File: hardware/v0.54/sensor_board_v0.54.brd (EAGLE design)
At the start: 56.4 x 41.7 mm, 59 parts, among them J3 USB-MICROB, J6 AVR_SPI_PRG_6PTH, U1 ATMEGA328P, U10 TSL2591, U3 OPA344, U4 RFM69HW, U5 FT231XS, U6 ADMP401, U8 MCP1703CB, U9 BMP280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

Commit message: BOM update
- Added MPN for 0.1 and 10uF
- Added I2C address and value for SHT35 on schematic
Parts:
- U2: value (none) -> SHT35
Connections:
- removed net A7: U1.22
- removed net D5: U1.9
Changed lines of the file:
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@@
 </element>
 <element name="C6" library="SparkFun-Capacitors" package="0805" value="0.1uF" x="4.2926" y="22.1234" smashed="yes" rot="R180">
-<attribute name="MPN" value="CC0805ZRY5V8BB105" x="4.2926" y="22.1234" size="1.778" layer="27" rot="R180" display="off"/>
+<attribute name="MPN" value="CC0805KRX7R9BB104" x="4.2926" y="22.1234" size="1.778" layer="27" rot="R180" display="off"/>
 <attribute name="NAME" x="2.4003" y="21.6154" size="0.6096" layer="121" font="vector" rot="R90"/>
 </element>
@@
 <attribute name="VALUE" x="51.308" y="21.7678" size="1.27" layer="27"/>
 </element>
-<element name="U2" library="Adafruit SHT31" package="SHT3X" value="" x="54.2544" y="43.7896" smashed="yes">
+<element name="U2" library="Adafruit SHT31" package="SHT3X" value="SHT35" x="54.2544" y="43.7896" smashed="yes">
 <attribute name="MPN" value="SHT35-DIS-B" x="54.2544" y="43.7896" size="1.778" layer="27" display="off"/>
 <attribute name="NAME" x="55.2754" y="45.5012" size="0.6096" layer="121" font="vector" align="bottom-center"/>
@@
 </element>
 <element name="C4" library="SparkFun-Capacitors" package="0805" value="10uF" x="4.2926" y="24.2316" smashed="yes" rot="R180">
-<attribute name="MPN" value="CC0805ZRY5V8BB105" x="4.2926" y="24.2316" size="1.778" layer="27" rot="R180" display="off"/>
+<attribute name="MPN" value="CC0805KKX5R6BB106" x="4.2926" y="24.2316" size="1.778" layer="27" rot="R180" display="off"/>
 <attribute name="NAME" x="1.7907" y="24.2062" size="0.6096" layer="121" font="vector" rot="R270" align="bottom-center"/>
 </element>
@@
 <wire x1="53.5432" y1="27.2796" x2="44.2468" y2="27.2796" width="0.1778" layer="16"/>
 </signal>
-<signal name="D5">
-<contactref element="U1" pad="9"/>
-</signal>
 <signal name="N$4">
 <contactref element="U1" pad="8"/>
@@
 <wire x1="12.0904" y1="34.2392" x2="6.35" y2="34.2392" width="0.1778" layer="16"/>
 </signal>
-<signal name="A7">
-<contactref element="U1" pad="22"/>
-</signal>
 <signal name="A0">

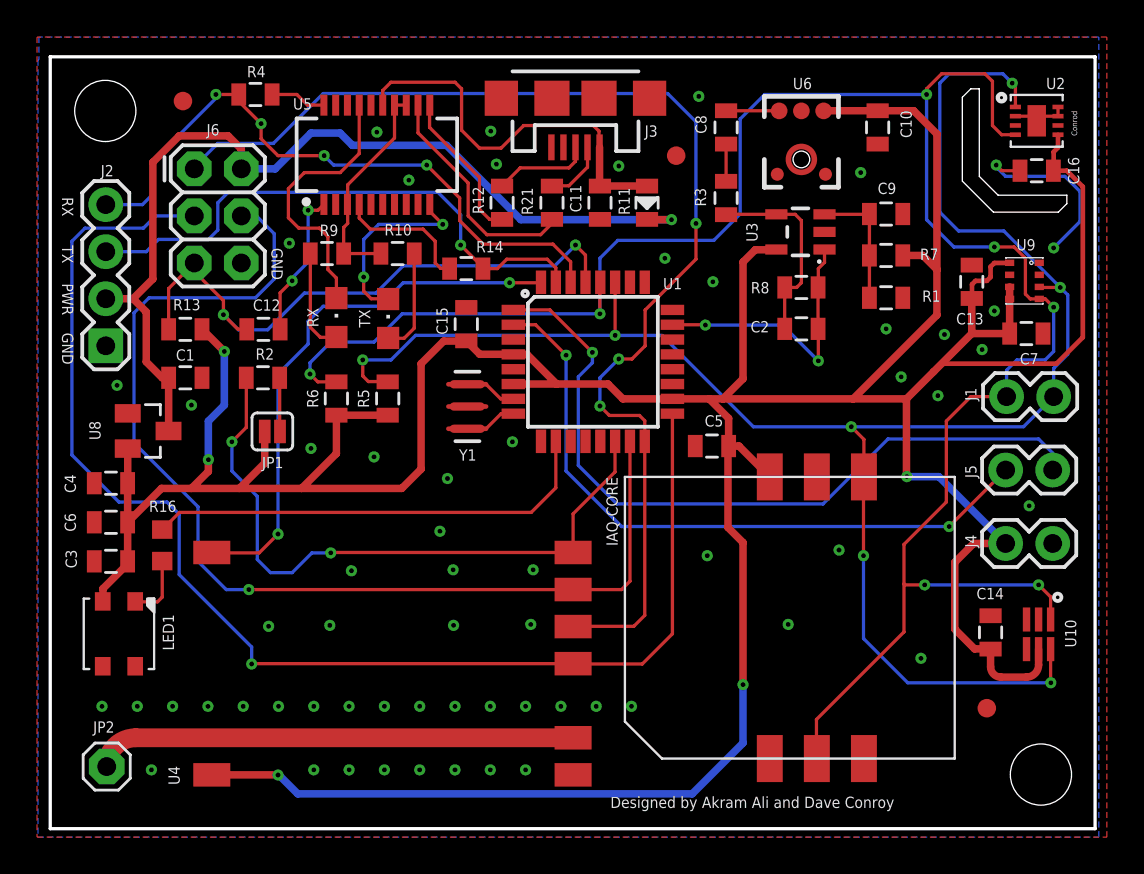
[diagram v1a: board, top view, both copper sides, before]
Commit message: trace adjustments
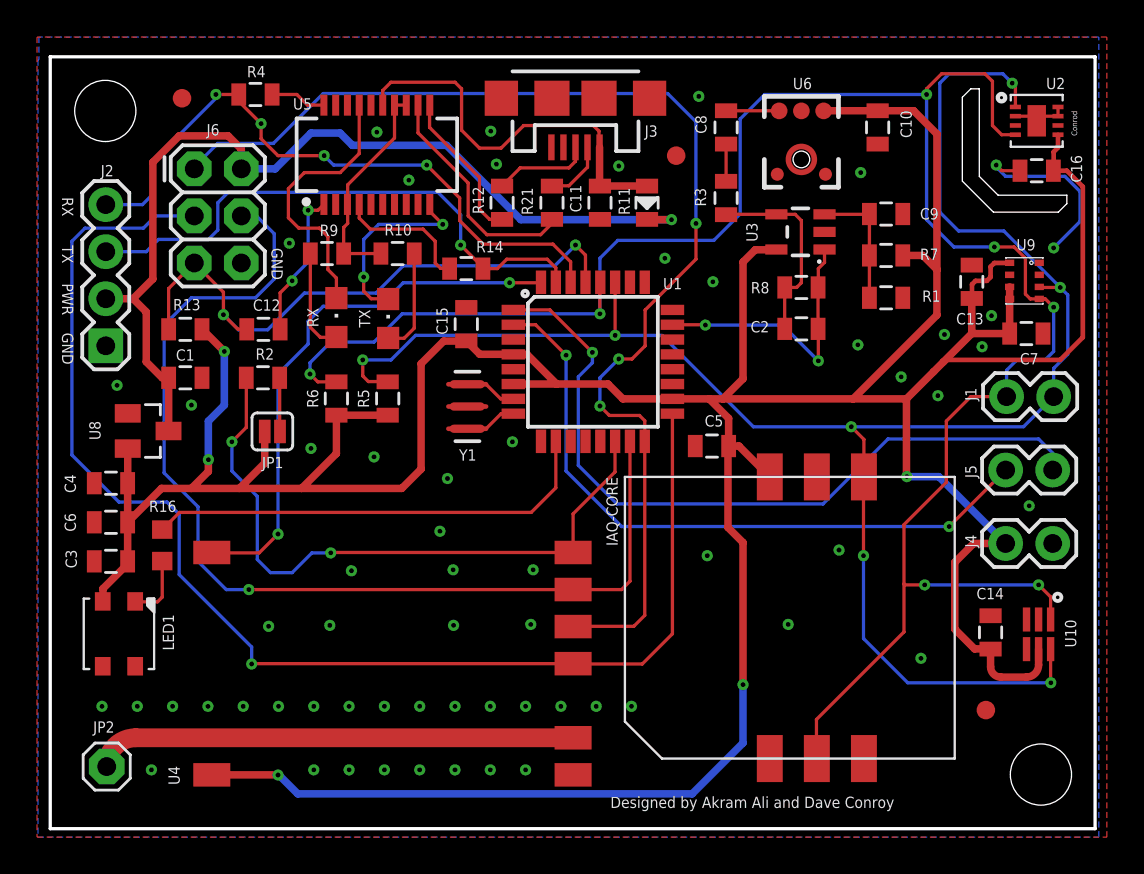
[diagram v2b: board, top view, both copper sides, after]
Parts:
- moved U$1 0.16 mm to (8.13, 45.0)
- moved U$2 0.11 mm to (51.5, 12.0)
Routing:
- net MOSI: track 59.5 -> 56.8 mm
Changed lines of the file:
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@@
 <?xml version="1.0" encoding="utf-8"?>
 <!DOCTYPE eagle SYSTEM "eagle.dtd">
-<eagle version="8.1.0">
+<eagle version="7.7.0">
 <drawing>
 <settings>
@@
 <element name="C9" library="SparkFun-Capacitors" package="0805" value="1uF" x="46.1264" y="38.7604" smashed="yes">
 <attribute name="MPN" value="CC0805ZRY5V8BB105" x="46.1264" y="38.7604" size="1.778" layer="27" display="off"/>
-<attribute name="NAME" x="45.6692" y="39.8399" size="0.6096" layer="121" font="vector"/>
+<attribute name="NAME" x="47.9552" y="38.4683" size="0.6096" layer="121" font="vector"/>
 </element>
 <element name="C10" library="SparkFun-Capacitors" package="0805" value="0.1uF" x="45.6692" y="43.434" smashed="yes" rot="R270">
@@
 <attribute name="VALUE" x="2.794" y="5.7658" size="1.27" layer="27"/>
 </element>
-<element name="U$1" library="adafruit" package="FIDUCIAL_1MM" value="FIDUCIAL" x="8.1788" y="44.8564"/>
-<element name="U$2" library="adafruit" package="FIDUCIAL_1MM" value="FIDUCIAL" x="51.562" y="12.0904"/>
+<element name="U$1" library="adafruit" package="FIDUCIAL_1MM" value="FIDUCIAL" x="8.128" y="45.0088"/>
+<element name="U$2" library="adafruit" package="FIDUCIAL_1MM" value="FIDUCIAL" x="51.5112" y="11.9888"/>
 <element name="U$3" library="adafruit" package="FIDUCIAL_1MM" value="FIDUCIAL" x="34.798" y="41.91"/>
 <element name="U10" library="TSL2591" package="DFN6_TAOS" value="TSL2591" x="54.356" y="16.0782" smashed="yes" rot="R270">
@@
 <element name="C16" library="SparkFun-Passives" package="0805" value="0.1uF" x="54.2544" y="41.0972" smashed="yes" rot="R180">
 <attribute name="MPN" value="CC0805KRX7R9BB104" x="54.2544" y="41.0972" size="1.778" layer="27" rot="R180" display="off"/>
-<attribute name="NAME" x="55.9435" y="41.0972" size="0.6096" layer="121" font="vector" rot="R270" align="bottom-center"/>
+<attribute name="NAME" x="56.0959" y="41.1988" size="0.6096" layer="121" font="vector" rot="R270" align="bottom-center"/>
 </element>
 <element name="J6" library="SparkFun-Connectors" package="2X3" value="AVR_SPI_PRG_6PTH" x="8.7884" y="41.1988" smashed="yes" rot="R270">
@@
 <via x="18.6436" y="43.18" extent="1-16" drill="0.254" diameter="0.127"/>
 <via x="49.276" y="32.258" extent="1-16" drill="0.254" diameter="0.127"/>
-<via x="46.1264" y="32.5628" extent="1-16" drill="0.254" diameter="0.127"/>
+<via x="44.6024" y="31.6992" extent="1-16" drill="0.254" diameter="0.127"/>
 <via x="48.9204" y="28.956" extent="1-16" drill="0.254" diameter="0.127"/>
 <via x="46.9392" y="29.972" extent="1-16" drill="0.254" diameter="0.127"/>
-<via x="51.308" y="31.4452" extent="1-16" drill="0.254" diameter="0.127"/>
+<via x="51.308" y="31.5976" extent="1-16" drill="0.254" diameter="0.127"/>
 <via x="24.7904" y="43.2308" extent="1-16" drill="0.254" diameter="0.127"/>
 <via x="25.0952" y="41.4528" extent="1-16" drill="0.254" diameter="0.127"/>
@@
 <via x="3.81" y="12.192" extent="1-16" drill="0.254" diameter="0.127"/>
 <via x="6.477" y="8.763" extent="1-16" drill="0.254" diameter="0.127"/>
-<via x="51.9684" y="33.528" extent="1-16" drill="0.254" diameter="0.127"/>
+<via x="51.816" y="33.274" extent="1-16" drill="0.254" diameter="0.127"/>
 <contactref element="U10" pad="3"/>
 <contactref element="C14" pad="1"/>
@@
 <wire x1="50.7636" y1="34.1884" x2="50.7492" y2="34.2028" width="0.4064" layer="1"/>
 <wire x1="47.2252" y1="28.7848" x2="48.6918" y2="30.2514" width="0.4064" layer="1"/>
-<wire x1="48.6918" y1="30.2514" x2="50.7492" y2="32.3088" width="0.4064" layer="1"/>
+<wire x1="48.6918" y1="30.2514" x2="49.2252" y2="30.7848" width="0.4064" layer="1"/>
+<wire x1="49.2252" y1="30.7848" x2="50.7492" y2="32.3088" width="0.4064" layer="1"/>
 <wire x1="45.6692" y1="44.334" x2="47.614" y2="44.334" width="0.4064" layer="1"/>
 <wire x1="47.614" y1="44.334" x2="48.8696" y2="43.0784" width="0.4064" layer="1"/>
@@
 <wire x1="55.1688" y1="42.1132" x2="55.1688" y2="41.1116" width="0.254" layer="1"/>
 <wire x1="55.1688" y1="41.1116" x2="55.1544" y2="41.0972" width="0.254" layer="1"/>
-<wire x1="55.3212" y1="30.6832" x2="49.1236" y2="30.6832" width="0.254" layer="1"/>
 <wire x1="49.1236" y1="30.6832" x2="48.6918" y2="30.2514" width="0.254" layer="1"/>
 <wire x1="47.2252" y1="28.7848" x2="47.2252" y2="24.606" width="0.4064" layer="1"/>
@@
 <wire x1="55.88" y1="41.0972" x2="56.7436" y2="40.2336" width="0.254" layer="1"/>
 <wire x1="56.7436" y1="40.2336" x2="56.7436" y2="32.1056" width="0.254" layer="1"/>
-<wire x1="56.7436" y1="32.1056" x2="55.3212" y2="30.6832" width="0.254" layer="1"/>
 <contactref element="C4" pad="1"/>
 <contactref element="C3" pad="1"/>
@@
 <wire x1="9.5504" y1="24.8666" x2="8.636" y2="23.9522" width="0.4064" layer="1"/>
 <wire x1="9.5504" y1="25.5016" x2="9.5504" y2="24.8666" width="0.4064" layer="1"/>
+<wire x1="56.7436" y1="32.1056" x2="55.5244" y2="30.8864" width="0.254" layer="1"/>
+<wire x1="55.5244" y1="30.8864" x2="49.3268" y2="30.8864" width="0.254" layer="1"/>
+<wire x1="49.3268" y1="30.8864" x2="49.2252" y2="30.7848" width="0.254" layer="1"/>
 </signal>
 <signal name="SCL">
@@
 <wire x1="52.6288" y1="28.9052" x2="50.6984" y2="28.9052" width="0.1778" layer="1"/>
 <wire x1="50.6984" y1="28.9052" x2="49.3776" y2="27.5844" width="0.1778" layer="1"/>
-<wire x1="49.3776" y1="27.5844" x2="49.3776" y2="23.2156" width="0.1778" layer="1"/>
-<wire x1="49.3776" y1="23.2156" x2="47.0916" y2="20.9296" width="0.1778" layer="1"/>
-<wire x1="47.0916" y1="20.9296" x2="47.0916" y2="18.796" width="0.1778" layer="1"/>
+<wire x1="47.0916" y1="21.9964" x2="47.0916" y2="18.796" width="0.1778" layer="1"/>
 <wire x1="47.0916" y1="18.796" x2="47.0916" y2="16.2052" width="0.1778" layer="1"/>
 <wire x1="47.0916" y1="16.2052" x2="42.3672" y2="11.4808" width="0.1778" layer="1"/>
@@
 <wire x1="51.8668" y1="45.9232" x2="51.4604" y2="46.3296" width="0.1778" layer="1"/>
 <wire x1="51.4604" y1="46.3296" x2="49.1236" y2="46.3296" width="0.1778" layer="1"/>
+<wire x1="47.0916" y1="21.9964" x2="49.3776" y2="24.2824" width="0.1778" layer="1"/>
+<wire x1="49.3776" y1="24.2824" x2="49.3776" y2="27.5844" width="0.1778" layer="1"/>
 </signal>
 <signal name="SDA">
@@
 <wire x1="29.9022" y1="36.5442" x2="29.9022" y2="35.0774" width="0.1778" layer="1"/>
 <contactref element="J6" pad="5"/>
-<wire x1="8.7376" y1="36.068" x2="8.7884" y2="36.1188" width="0.1778" layer="16"/>
 <wire x1="18.5928" y1="34.4932" x2="14.732" y2="34.4932" width="0.1778" layer="16"/>
-<wire x1="8.7884" y1="36.1188" x2="8.7884" y2="35.6616" width="0.1778" layer="1"/>
-<wire x1="8.7884" y1="35.6616" x2="10.3632" y2="34.0868" width="0.1778" layer="1"/>
 <wire x1="7.4058" y1="32.5374" x2="7.4058" y2="34.7362" width="0.1778" layer="1"/>
-<wire x1="7.4058" y1="34.7362" x2="8.7884" y2="36.1188" width="0.1778" layer="1"/>
 <wire x1="14.732" y1="34.4932" x2="12.7508" y2="32.512" width="0.1778" layer="16"/>
 <wire x1="12.7508" y1="32.512" x2="11.176" y2="32.512" width="0.1778" layer="16"/>
 <wire x1="11.176" y1="32.512" x2="10.3632" y2="33.3248" width="0.1778" layer="16"/>
 <via x="10.3632" y="33.3248" extent="1-16" drill="0.254" diameter="0.127"/>
-<wire x1="10.3632" y1="33.3248" x2="10.3632" y2="34.0868" width="0.1778" layer="1"/>
+<wire x1="10.3632" y1="33.3248" x2="10.3632" y2="34.544" width="0.1778" layer="1"/>
 <wire x1="11.6222" y1="32.5374" x2="11.1506" y2="32.5374" width="0.1778" layer="1"/>
 <wire x1="11.1506" y1="32.5374" x2="10.3632" y2="33.3248" width="0.1778" layer="1"/>
@@
 <wire x1="20.066" y1="35.9664" x2="28.2448" y2="35.9664" width="0.1778" layer="16"/>
 <wire x1="28.2448" y1="35.9664" x2="29.3624" y2="37.084" width="0.1778" layer="16"/>
+<wire x1="8.7884" y1="36.1188" x2="10.3632" y2="34.544" width="0.1778" layer="1"/>
+<wire x1="8.7884" y1="36.1188" x2="7.4058" y2="34.7362" width="0.1778" layer="1"/>
 </signal>
 <signal name="MOSI">
@@
 <via x="11.7348" y="18.4912" extent="1-16" drill="0.254" diameter="0.127"/>
 <wire x1="10.5156" y1="18.4912" x2="11.7348" y2="18.4912" width="0.1778" layer="16"/>
-<wire x1="5.5372" y1="33.4264" x2="5.5372" y2="26.416" width="0.1778" layer="16"/>
 <wire x1="31.8516" y1="18.4912" x2="29.2372" y2="18.4912" width="0.1778" layer="1"/>
 <wire x1="29.2372" y1="18.4912" x2="29.2344" y2="18.494" width="0.1778" layer="1"/>
@@
 <contactref element="J6" pad="4"/>
 <wire x1="11.3284" y1="38.7096" x2="11.3284" y2="38.6588" width="0.1778" layer="16"/>
-<wire x1="6.35" y1="34.2392" x2="5.5372" y2="33.4264" width="0.1778" layer="16"/>
-<wire x1="5.5372" y1="26.416" x2="8.9916" y2="22.9616" width="0.1778" layer="16"/>
 <wire x1="8.9916" y1="22.9616" x2="8.9916" y2="20.0152" width="0.1778" layer="16"/>
 <wire x1="11.3284" y1="38.6588" x2="12.1412" y2="38.6588" width="0.1778" layer="16"/>
@@
 <wire x1="13.1064" y1="37.6936" x2="13.1064" y2="35.2552" width="0.1778" layer="16"/>
 <wire x1="13.1064" y1="35.2552" x2="12.0904" y2="34.2392" width="0.1778" layer="16"/>
-<wire x1="12.0904" y1="34.2392" x2="6.35" y2="34.2392" width="0.1778" layer="16"/>
+<wire x1="12.0904" y1="34.2392" x2="8.636" y2="34.2392" width="0.1778" layer="16"/>
+<wire x1="8.636" y1="34.2392" x2="7.1628" y2="32.766" width="0.1778" layer="16"/>
+<wire x1="7.1628" y1="32.766" x2="7.1628" y2="24.7904" width="0.1778" layer="16"/>
+<wire x1="7.1628" y1="24.7904" x2="8.9916" y2="22.9616" width="0.1778" layer="16"/>
 </signal>
 <signal name="A0">

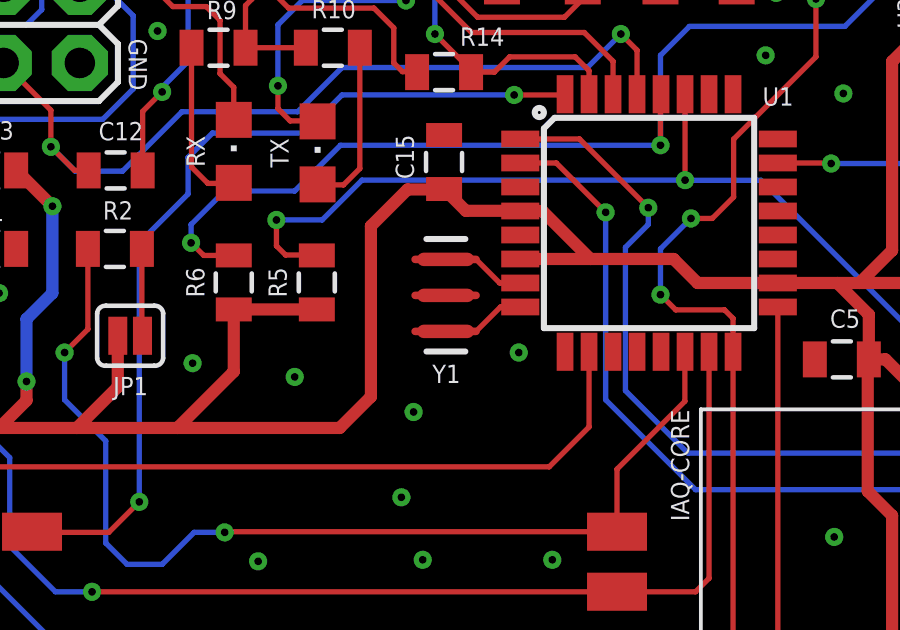
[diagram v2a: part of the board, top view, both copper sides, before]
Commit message: v0.54 update - resonator library changed
- Replaced previous resonator library (thinner pads, incorrectly
aligned, usually got lucky) with one that has fatter pads (from RFM69
USB gateway)
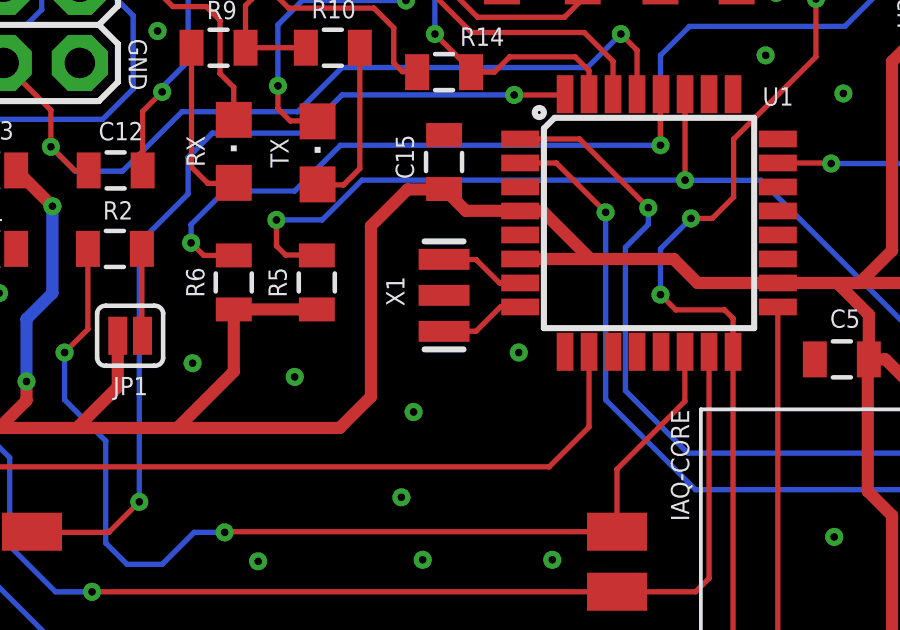
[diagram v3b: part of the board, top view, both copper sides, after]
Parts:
- removed Y1: 16MHZ, SparkFun-FreqCtrl:RESONATOR-SMD
- added X1: 16 MHz, SparkFun:RESONATOR-SMD
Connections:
- net GND: now also X1.2; no longer Y1.2
- net N$4: now also X1.3; no longer Y1.3
- net N$5: now also X1.1; no longer Y1.1
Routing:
- net N$5: track 1.80 -> 2.87 mm
- net N$4: track 1.81 -> 2.88 mm
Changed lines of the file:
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@@
 <?xml version="1.0" encoding="utf-8"?>
 <!DOCTYPE eagle SYSTEM "eagle.dtd">
-<eagle version="7.7.0">
+<eagle version="8.1.0">
 <drawing>
 <settings>
@@
 <class number="0" name="default" width="0" drill="0">
 </class>
+<class number="1" name="power" width="0.381" drill="0">
+<clearance class="1" value="0.254"/>
+</class>
 </classes>
 <designrules name="oshpark-2layer">
@@
 <attribute name="NAME" x="37.338" y="27.9019" size="0.6096" layer="121" font="vector" rot="R180"/>
 </element>
-<element name="Y1" library="SparkFun-FreqCtrl" package="RESONATOR-SMD" value="16MHZ" x="23.5204" y="28.3718" smashed="yes" rot="R270">
-<attribute name="MF" value="" x="23.5204" y="28.3718" size="1.778" layer="27" rot="R270" display="off"/>
-<attribute name="MPN" value="CSTCE16M0V53-R0" x="23.5204" y="28.3718" size="1.778" layer="27" rot="R270" display="off"/>
-<attribute name="NAME" x="23.5458" y="25.4508" size="0.6096" layer="121" font="vector" align="bottom-center"/>
-<attribute name="OC_NEWARK" value="unknown" x="23.5204" y="28.3718" size="1.778" layer="27" rot="R270" display="off"/>
-<attribute name="PROD_ID" value="XTAL-08900" x="23.5204" y="28.3718" size="1.778" layer="27" rot="R270" display="off"/>
-</element>
 <element name="U8" library="linear" package="SOT23" value="MCP1703CB" x="6.2992" y="27.051" smashed="yes" rot="R270">
 <attribute name="MF" value="" x="6.2992" y="27.051" size="1.778" layer="27" rot="R270" display="off"/>
@@
 <attribute name="NAME" x="1.8415" y="20.1422" size="0.6096" layer="121" font="vector" rot="R270" align="bottom-center"/>
 </element>
+<element name="X1" library="SparkFun" package="RESONATOR-SMD" value="16 MHz" x="23.4696" y="28.3718" smashed="yes" rot="R270">
+<attribute name="NAME" x="21.5392" y="29.0068" size="0.6096" layer="121" font="vector" rot="R270"/>
+</element>
 </elements>
 <signals>
@@
 <contactref element="U1" pad="3"/>
 <contactref element="U1" pad="21"/>
-<contactref element="Y1" pad="2"/>
 <contactref element="C1" pad="2"/>
 <contactref element="U8" pad="1"/>
@@
 <contactref element="C4" pad="2"/>
 <contactref element="C3" pad="2"/>
+<contactref element="X1" pad="2"/>
 </signal>
 <signal name="VCC">
@@
 <signal name="N$4">
 <contactref element="U1" pad="8"/>
-<contactref element="Y1" pad="3"/>
-<wire x1="26.0096" y1="27.9848" x2="25.3494" y2="27.9848" width="0.1778" layer="1"/>
-<wire x1="25.3494" y1="27.9848" x2="24.5364" y2="27.1718" width="0.1778" layer="1"/>
+<contactref element="X1" pad="3"/>
+<wire x1="25.3432" y1="27.9848" x2="24.5364" y2="27.178" width="0.1778" layer="1"/>
+<wire x1="24.5364" y1="27.178" x2="23.4758" y2="27.178" width="0.1778" layer="1"/>
+<wire x1="23.4758" y1="27.178" x2="23.4696" y2="27.1718" width="0.1778" layer="1"/>
+<wire x1="26.0096" y1="27.9848" x2="25.3432" y2="27.9848" width="0.1778" layer="1"/>
 </signal>
 <signal name="N$5">
 <contactref element="U1" pad="7"/>
-<contactref element="Y1" pad="1"/>
-<wire x1="26.0096" y1="28.7848" x2="25.3234" y2="28.7848" width="0.1778" layer="1"/>
-<wire x1="25.3234" y1="28.7848" x2="24.5364" y2="29.5718" width="0.1778" layer="1"/>
+<contactref element="X1" pad="1"/>
+<wire x1="25.3172" y1="28.7848" x2="24.5364" y2="29.5656" width="0.1778" layer="1"/>
+<wire x1="24.5364" y1="29.5656" x2="23.4758" y2="29.5656" width="0.1778" layer="1"/>
+<wire x1="23.4758" y1="29.5656" x2="23.4696" y2="29.5718" width="0.1778" layer="1"/>
+<wire x1="26.0096" y1="28.7848" x2="25.3172" y2="28.7848" width="0.1778" layer="1"/>
 </signal>
 <signal name="PWR">
